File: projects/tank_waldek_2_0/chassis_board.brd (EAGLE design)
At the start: 100 x 60 mm, 22 parts, among them U1 NUCLEO-L432KC

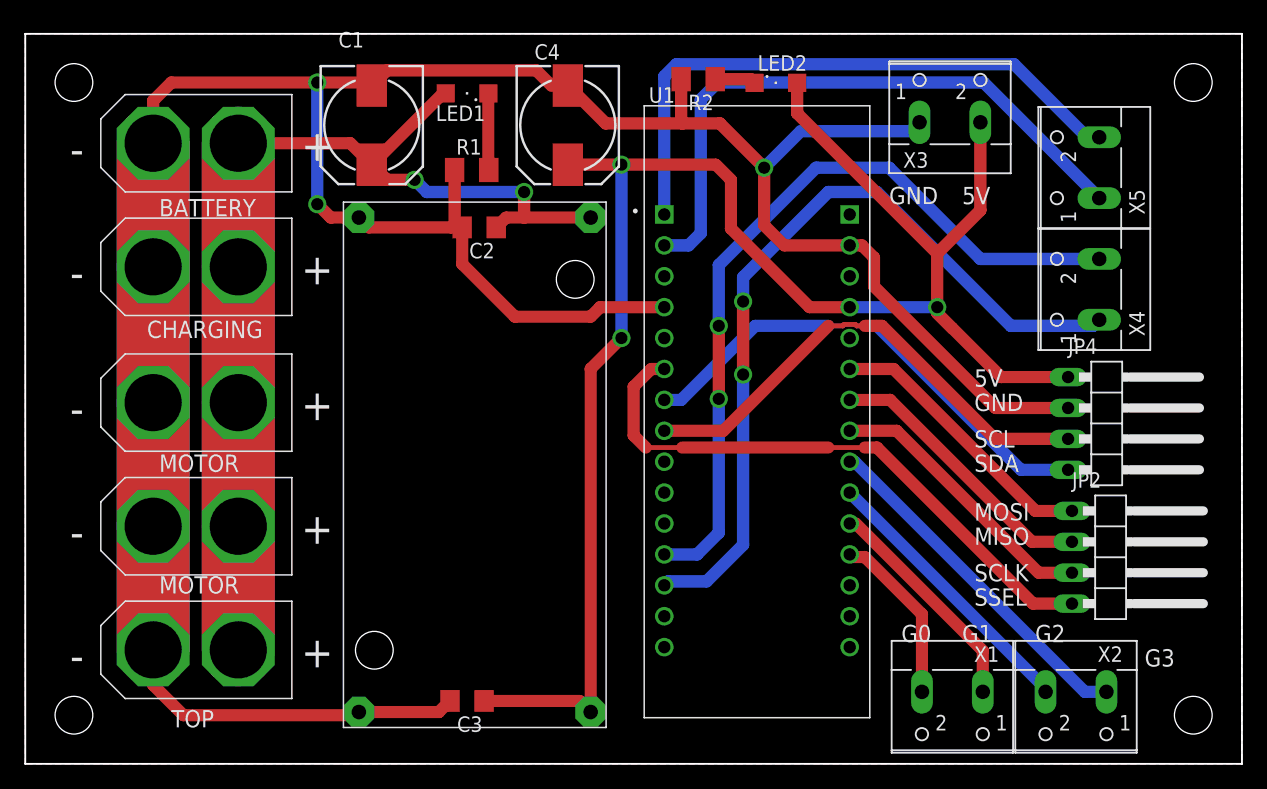
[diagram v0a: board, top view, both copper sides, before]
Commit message: updated waldek chassis board and added new rpi shield
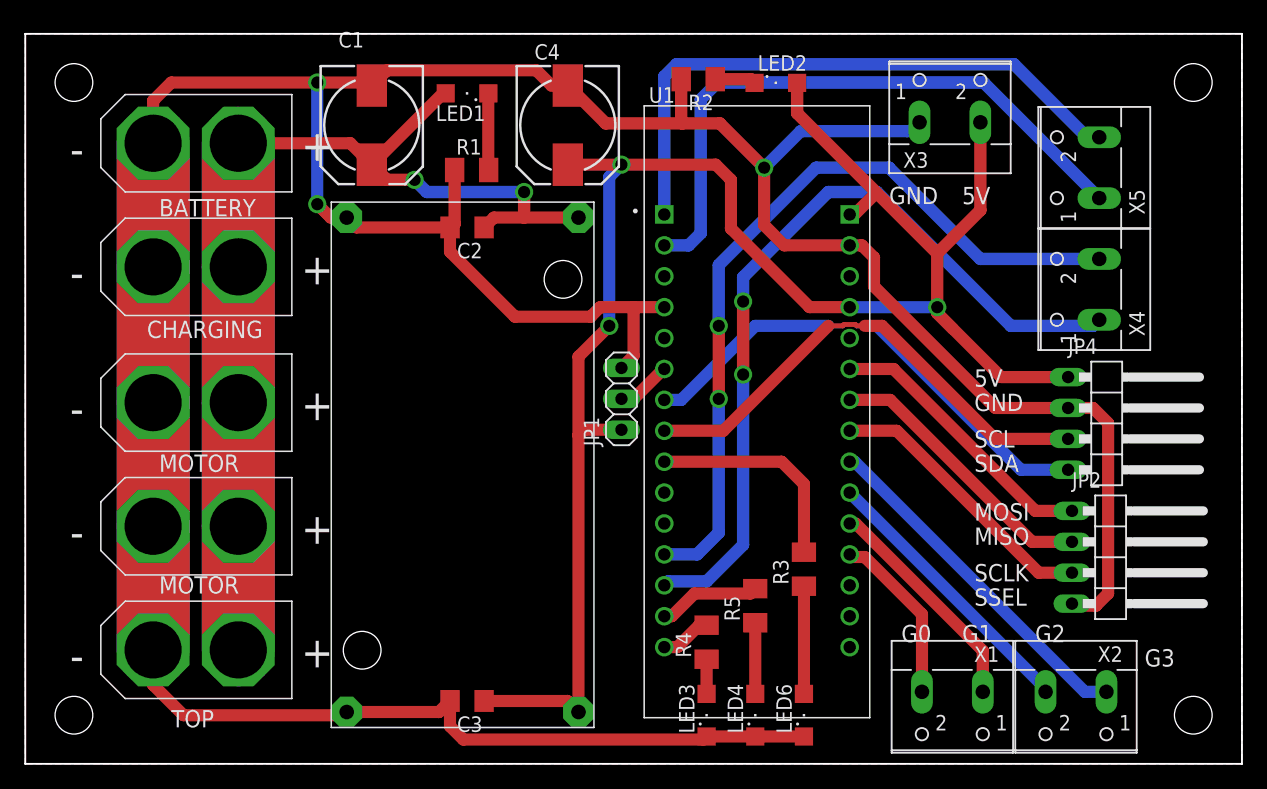
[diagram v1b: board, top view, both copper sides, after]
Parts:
- added JP1: (no value), pinhead:1X03
- added LED3, LED4, LED6: (no value), led:SML1206
- added R3, R4, R5: (no value), rcl:M1206
- moved C2 1.00 mm to (36.3, 44.1)
- moved U$6 1.00 mm to (25.1, 2.99)
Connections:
- new net LED_0: R3.2, U1.CN3_9
- new net LED_1: R4.2, U1.CN3_15
- new net LED_2: R5.2, U1.CN3_14
- new net N$3: LED6.A, R3.1
- new net N$7: LED3.A, R4.1
- new net N$8: LED4.A, R5.1
- net GND: now also JP1.3, JP2.4, LED3.C, LED4.C, LED6.C
- net SSEL: now also JP1.2; no longer JP2.4
- net VCC: now also JP1.1, U1.CN4_1
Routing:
- net GND: track 274.9 -> 332.8 mm
- net SSEL: track 48.9 -> 4.54 mm
- net LED_0: track 0.00 -> 17.8 mm
- net N$3: track 0.00 -> 8.85 mm
- net LED_2: track 0.00 -> 8.42 mm
- net VCC: track 141.6 -> 147.7 mm
- net N$8: track 0.00 -> 5.85 mm
- net LED_1: track 0.00 -> 4.23 mm
- net N$7: track 0.00 -> 2.85 mm

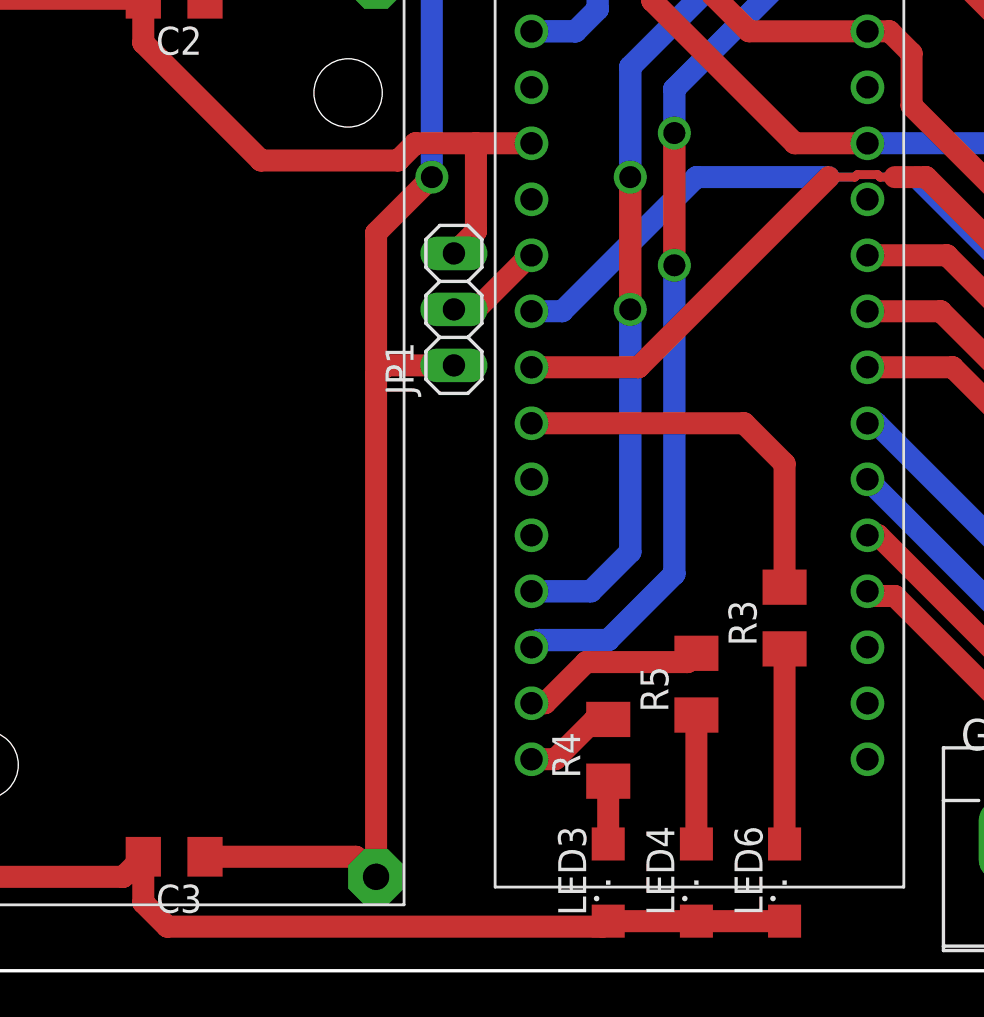
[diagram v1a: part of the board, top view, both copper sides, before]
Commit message: minor fixes of waldek 2 chassis board and rpi shield
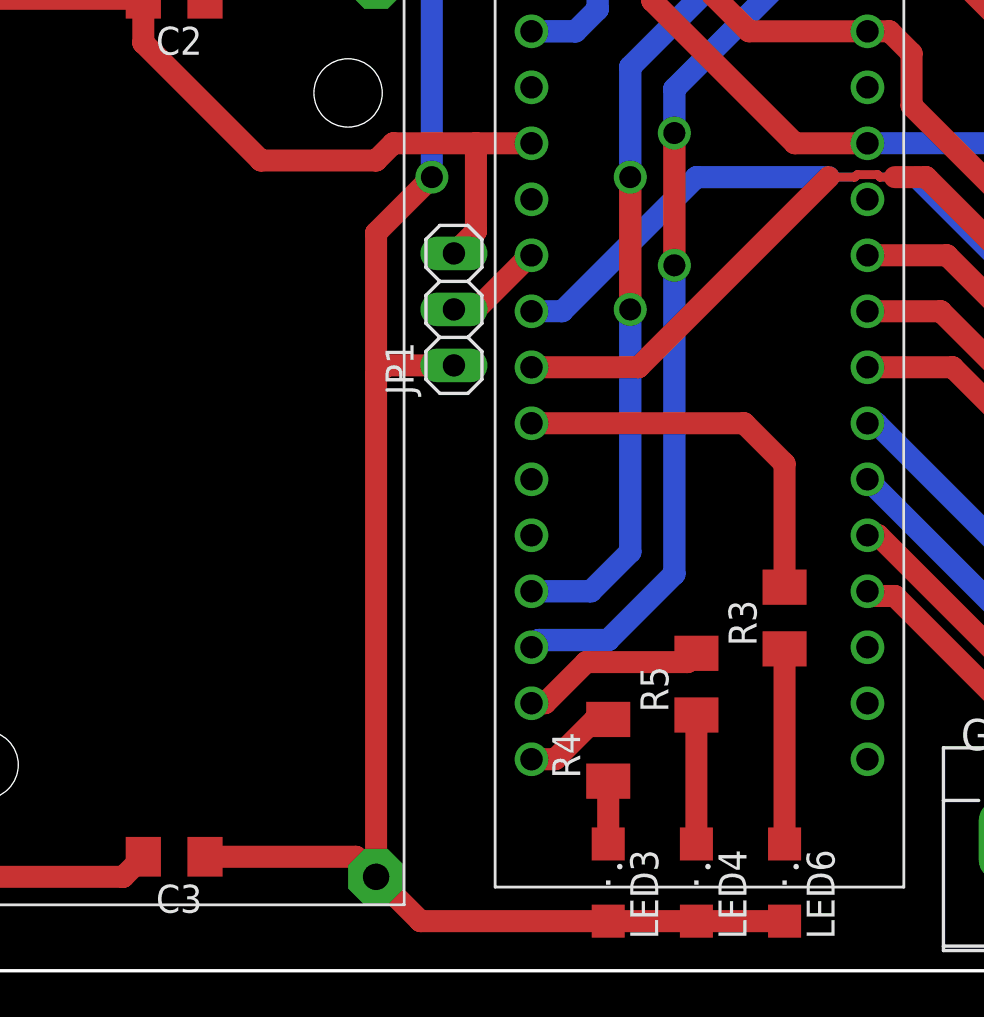
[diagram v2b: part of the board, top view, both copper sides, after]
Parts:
- turned LED3 to 270 degrees
- turned LED4 to 270 degrees
- turned LED6 to 270 degrees
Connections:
- net GND: no longer LED3.C, LED4.C, LED6.C
- net N$3: now also LED6.C; no longer LED6.A
- net N$7: now also LED3.C; no longer LED3.A
- net N$8: now also LED4.C; no longer LED4.A
- net VCC: now also LED3.A, LED4.A, LED6.A
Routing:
- net GND: track 332.8 -> 301.1 mm
- net VCC: track 147.7 -> 167.0 mm
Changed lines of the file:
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@@
 <attribute name="VALUE" x="52.175" y="26.19" size="1.27" layer="27" rot="R90"/>
 </element>
-<element name="LED6" library="led" library_urn="urn:adsk.eagle:library:259" package="SML1206" package3d_urn="urn:adsk.eagle:package:15829/1" value="" x="64" y="4" smashed="yes" rot="R90">
-<attribute name="NAME" x="63" y="2.5" size="1.27" layer="25" rot="R90"/>
-<attribute name="POPULARITY" value="6" x="64" y="4" size="1.778" layer="27" rot="R90" display="off"/>
-<attribute name="VALUE" x="66.5" y="2.5" size="1.27" layer="27" rot="R90"/>
+<element name="LED6" library="led" library_urn="urn:adsk.eagle:library:259" package="SML1206" package3d_urn="urn:adsk.eagle:package:15829/1" value="" x="64" y="4" smashed="yes" rot="R270">
+<attribute name="NAME" x="65" y="5.5" size="1.27" layer="25" rot="R270"/>
+<attribute name="POPULARITY" value="6" x="64" y="4" size="1.778" layer="27" rot="R270" display="off"/>
+<attribute name="VALUE" x="61.5" y="5.5" size="1.27" layer="27" rot="R270"/>
 </element>
-<element name="LED3" library="led" library_urn="urn:adsk.eagle:library:259" package="SML1206" package3d_urn="urn:adsk.eagle:package:15829/1" value="" x="56" y="4" smashed="yes" rot="R90">
-<attribute name="NAME" x="55" y="2.5" size="1.27" layer="25" rot="R90"/>
-<attribute name="POPULARITY" value="6" x="56" y="4" size="1.778" layer="27" rot="R90" display="off"/>
-<attribute name="VALUE" x="58.5" y="2.5" size="1.27" layer="27" rot="R90"/>
+<element name="LED3" library="led" library_urn="urn:adsk.eagle:library:259" package="SML1206" package3d_urn="urn:adsk.eagle:package:15829/1" value="" x="56" y="4" smashed="yes" rot="R270">
+<attribute name="NAME" x="57" y="5.5" size="1.27" layer="25" rot="R270"/>
+<attribute name="POPULARITY" value="6" x="56" y="4" size="1.778" layer="27" rot="R270" display="off"/>
+<attribute name="VALUE" x="53.5" y="5.5" size="1.27" layer="27" rot="R270"/>
 </element>
-<element name="LED4" library="led" library_urn="urn:adsk.eagle:library:259" package="SML1206" package3d_urn="urn:adsk.eagle:package:15829/1" value="" x="60" y="4" smashed="yes" rot="R90">
-<attribute name="NAME" x="59" y="2.5" size="1.27" layer="25" rot="R90"/>
-<attribute name="POPULARITY" value="6" x="60" y="4" size="1.778" layer="27" rot="R90" display="off"/>
-<attribute name="VALUE" x="62.5" y="2.5" size="1.27" layer="27" rot="R90"/>
+<element name="LED4" library="led" library_urn="urn:adsk.eagle:library:259" package="SML1206" package3d_urn="urn:adsk.eagle:package:15829/1" value="" x="60" y="4" smashed="yes" rot="R270">
+<attribute name="NAME" x="61" y="5.5" size="1.27" layer="25" rot="R270"/>
+<attribute name="POPULARITY" value="6" x="60" y="4" size="1.778" layer="27" rot="R270" display="off"/>
+<attribute name="VALUE" x="57.5" y="5.5" size="1.27" layer="27" rot="R270"/>
 </element>
 </elements>
@@
 <wire x1="29.73" y1="57" x2="28.48" y2="55.75" width="1" layer="1"/>
 <wire x1="52.52" y1="37.535" x2="50" y2="37.535" width="1" layer="1"/>
-<wire x1="50" y1="37.535" x2="47.25098125" y2="37.535" width="1" layer="1"/>
-<wire x1="47.25098125" y1="37.535" x2="46.46998125" y2="36.754" width="1" layer="1"/>
-<wire x1="46.46998125" y1="36.754" x2="40.246" y2="36.754" width="1" layer="1"/>
+<wire x1="50" y1="37.535" x2="46.25098125" y2="37.535" width="1" layer="1"/>
+<wire x1="46.25098125" y1="37.535" x2="45.46998125" y2="36.754" width="1" layer="1"/>
+<wire x1="45.46998125" y1="36.754" x2="40.246" y2="36.754" width="1" layer="1"/>
 <wire x1="34.91" y1="42.09" x2="34.91" y2="44.09" width="1" layer="1"/>
 <wire x1="40.246" y1="36.754" x2="34.91" y2="42.09" width="1" layer="1"/>
@@
 <wire x1="89" y1="28" x2="87.75" y2="29.25" width="1" layer="1"/>
 <wire x1="87.75" y1="29.25" x2="85.71" y2="29.25" width="1" layer="1"/>
-<contactref element="LED6" pad="C"/>
-<contactref element="LED3" pad="C"/>
-<contactref element="LED4" pad="C"/>
-<wire x1="64" y1="2.25" x2="60" y2="2.25" width="1" layer="1"/>
-<wire x1="60" y1="2.25" x2="56" y2="2.25" width="1" layer="1"/>
-<wire x1="56" y1="2.25" x2="55.75" y2="2" width="1" layer="1"/>
-<wire x1="55.75" y1="2" x2="36" y2="2" width="1" layer="1"/>
-<wire x1="36" y1="2" x2="34.91" y2="3.09" width="1" layer="1"/>
-<wire x1="34.91" y1="3.09" x2="34.91" y2="5.17" width="1" layer="1"/>
 <wire x1="49" y1="32.54" x2="50" y2="33.54" width="1" layer="1"/>
 <wire x1="50" y1="33.54" x2="50" y2="37.535" width="1" layer="1"/>
@@
 <wire x1="67.76" y1="45.155" x2="68.155" y2="45.155" width="1" layer="1"/>
 <wire x1="68.155" y1="45.155" x2="69.955" y2="46.955" width="1" layer="1"/>
+<contactref element="LED4" pad="A"/>
+<contactref element="LED3" pad="A"/>
+<contactref element="LED6" pad="A"/>
+<wire x1="45.47" y1="4.26" x2="47.48" y2="2.25" width="1" layer="1"/>
+<wire x1="47.48" y1="2.25" x2="56" y2="2.25" width="1" layer="1"/>
+<wire x1="56" y1="2.25" x2="60" y2="2.25" width="1" layer="1"/>
+<wire x1="60" y1="2.25" x2="64" y2="2.25" width="1" layer="1"/>
 </signal>
 <signal name="N$1">
@@
 <signal name="N$3">
 <contactref element="R3" pad="1"/>
-<contactref element="LED6" pad="A"/>
-<wire x1="64" y1="14.6" x2="64" y2="5.75" width="1" layer="1"/>
+<contactref element="LED6" pad="C"/>
+<wire x1="64" y1="5.75" x2="64" y2="14.6" width="1" layer="1"/>
 </signal>
 <signal name="N$7">
 <contactref element="R4" pad="1"/>
-<contactref element="LED3" pad="A"/>
-<wire x1="56" y1="8.6" x2="56" y2="5.75" width="1" layer="1"/>
+<contactref element="LED3" pad="C"/>
+<wire x1="56" y1="5.75" x2="56" y2="8.6" width="1" layer="1"/>
 </signal>
 <signal name="N$8">
 <contactref element="R5" pad="1"/>
-<contactref element="LED4" pad="A"/>
-<wire x1="60" y1="11.6" x2="60" y2="5.75" width="1" layer="1"/>
+<contactref element="LED4" pad="C"/>
+<wire x1="60" y1="5.75" x2="60" y2="11.6" width="1" layer="1"/>
 </signal>
 </signals>
